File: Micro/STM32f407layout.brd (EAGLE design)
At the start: 100.1 x 96.7 mm, 69 parts, among them Q1 ASF, T3 FDN340P, T4 AP1117_LIN_REG

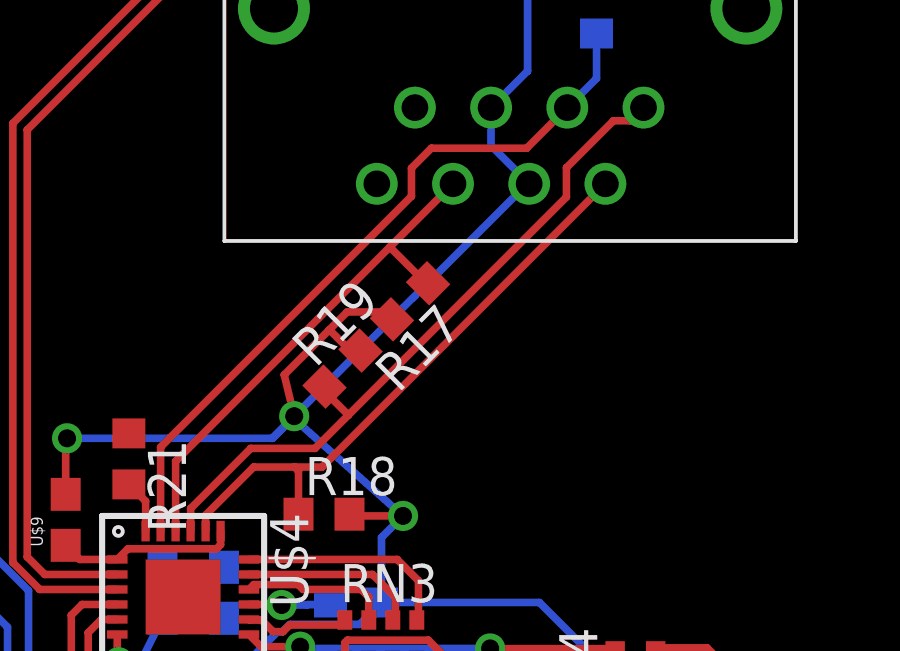
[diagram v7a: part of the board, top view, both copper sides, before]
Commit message: Ethernet Length Checks
Checked length of ethernet signals, still need to check tolerances on
RD+- and TD+-
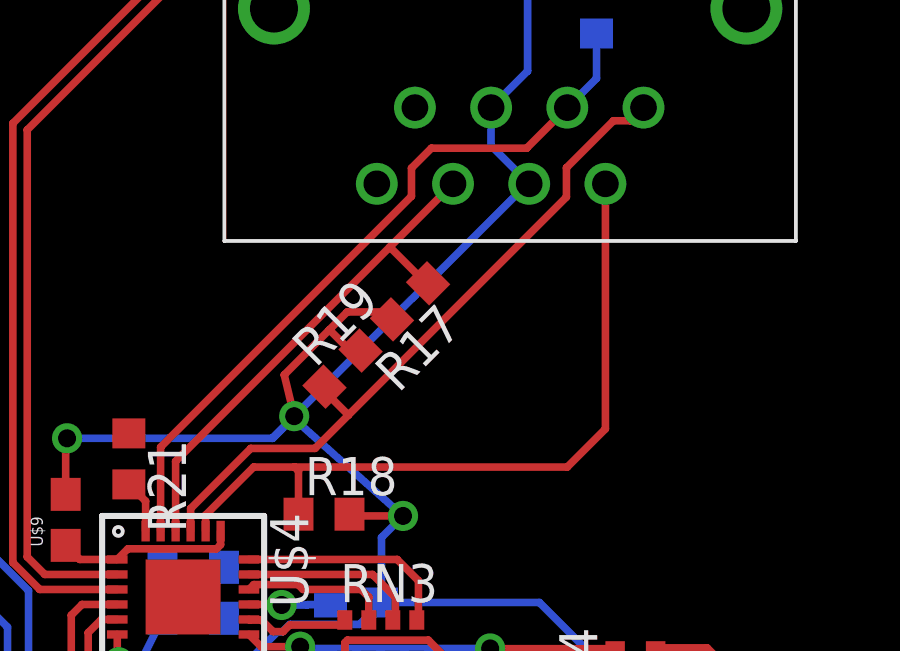
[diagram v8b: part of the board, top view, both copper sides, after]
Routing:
- net TD-: track 20.1 -> 24.8 mm
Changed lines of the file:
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@@
 <layer number="23" name="tOrigins" color="15" fill="1" visible="yes" active="yes"/>
 <layer number="24" name="bOrigins" color="15" fill="1" visible="yes" active="yes"/>
-<layer number="25" name="tNames" color="7" fill="1" visible="yes" active="yes"/>
-<layer number="26" name="bNames" color="7" fill="1" visible="yes" active="yes"/>
-<layer number="27" name="tValues" color="7" fill="1" visible="yes" active="yes"/>
-<layer number="28" name="bValues" color="7" fill="1" visible="yes" active="yes"/>
+<layer number="25" name="tNames" color="7" fill="1" visible="no" active="yes"/>
+<layer number="26" name="bNames" color="7" fill="1" visible="no" active="yes"/>
+<layer number="27" name="tValues" color="7" fill="1" visible="no" active="yes"/>
+<layer number="28" name="bValues" color="7" fill="1" visible="no" active="yes"/>
 <layer number="29" name="tStop" color="7" fill="3" visible="yes" active="yes"/>
 <layer number="30" name="bStop" color="7" fill="6" visible="yes" active="yes"/>
@@
 <wire x1="41.939528125" y1="52.688603125" x2="43.540146875" y2="54.289221875" width="0.254" layer="1"/>
 <wire x1="43.540146875" y1="54.289221875" x2="44.9056" y2="54.289221875" width="0.254" layer="1"/>
-<wire x1="44.9056" y1="54.289221875" x2="45.82478125" y2="54.289221875" width="0.254" layer="1"/>
-<wire x1="45.82478125" y1="54.289221875" x2="55.2664375" y2="63.730878125" width="0.254" layer="1"/>
 <wire x1="45.036109375" y1="52.71815625" x2="45.036109375" y2="54.1587125" width="0.254" layer="1"/>
 <wire x1="45.036109375" y1="54.1587125" x2="44.9056" y2="54.289221875" width="0.254" layer="1"/>
+<wire x1="44.9056" y1="54.289221875" x2="53.995165625" y2="54.289221875" width="0.254" layer="1"/>
+<wire x1="53.995165625" y1="54.289221875" x2="55.2664375" y2="55.56049375" width="0.254" layer="1"/>
+<wire x1="55.2664375" y1="63.730878125" x2="55.2664375" y2="55.56049375" width="0.254" layer="1"/>
 </signal>
 <signal name="NRST">
